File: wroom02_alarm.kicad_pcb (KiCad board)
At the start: 2 copper layers, 50 x 50 mm, 93 parts, among them J1 Serial, J10 pin, J11 pin, J12 pin, J13 pin, J14 pin, J15 pin, J2 pin, J3 microUSB, J4 pin, J5 pin, J6 pin, J7 pin, J8 pin, J9 pin, Q1 Q_NMOS_GDS, SW1 Write, SW2 RESET, U1 wroom02, U3 7803

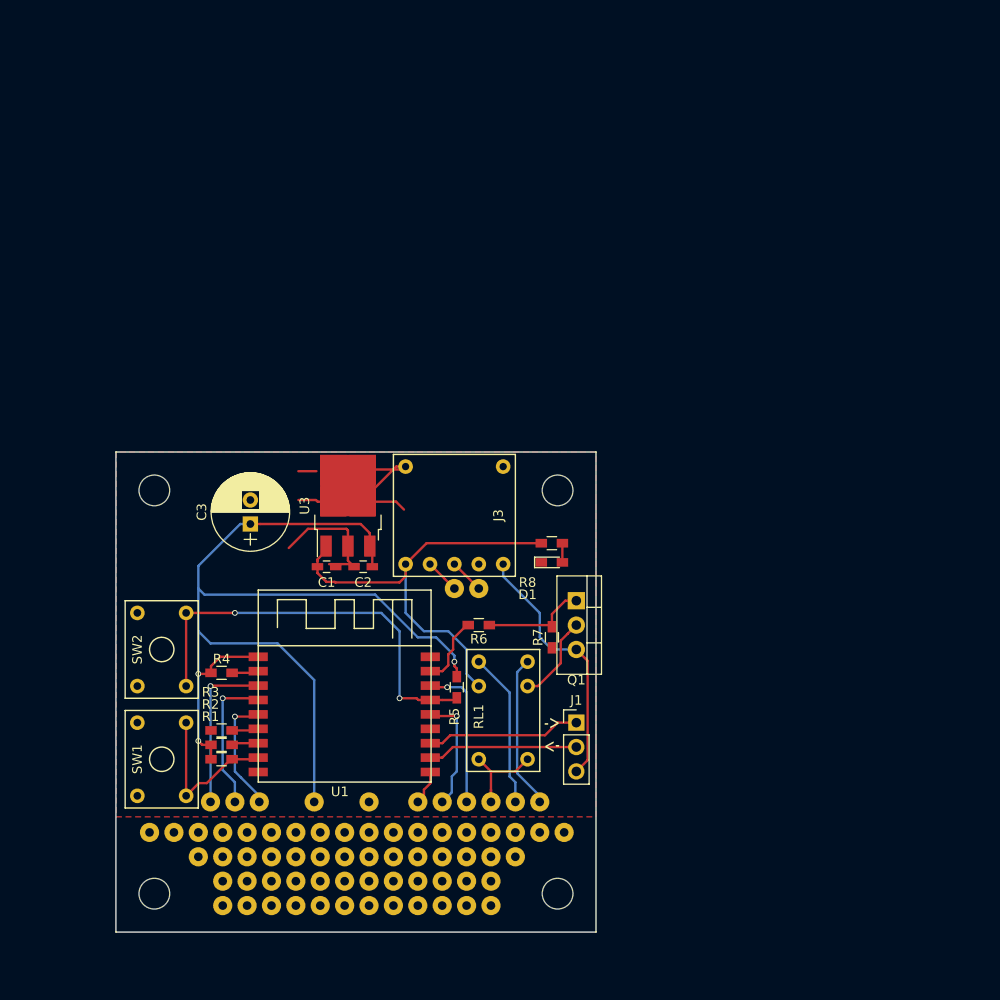
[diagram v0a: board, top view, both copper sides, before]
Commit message: 100x100に拡張
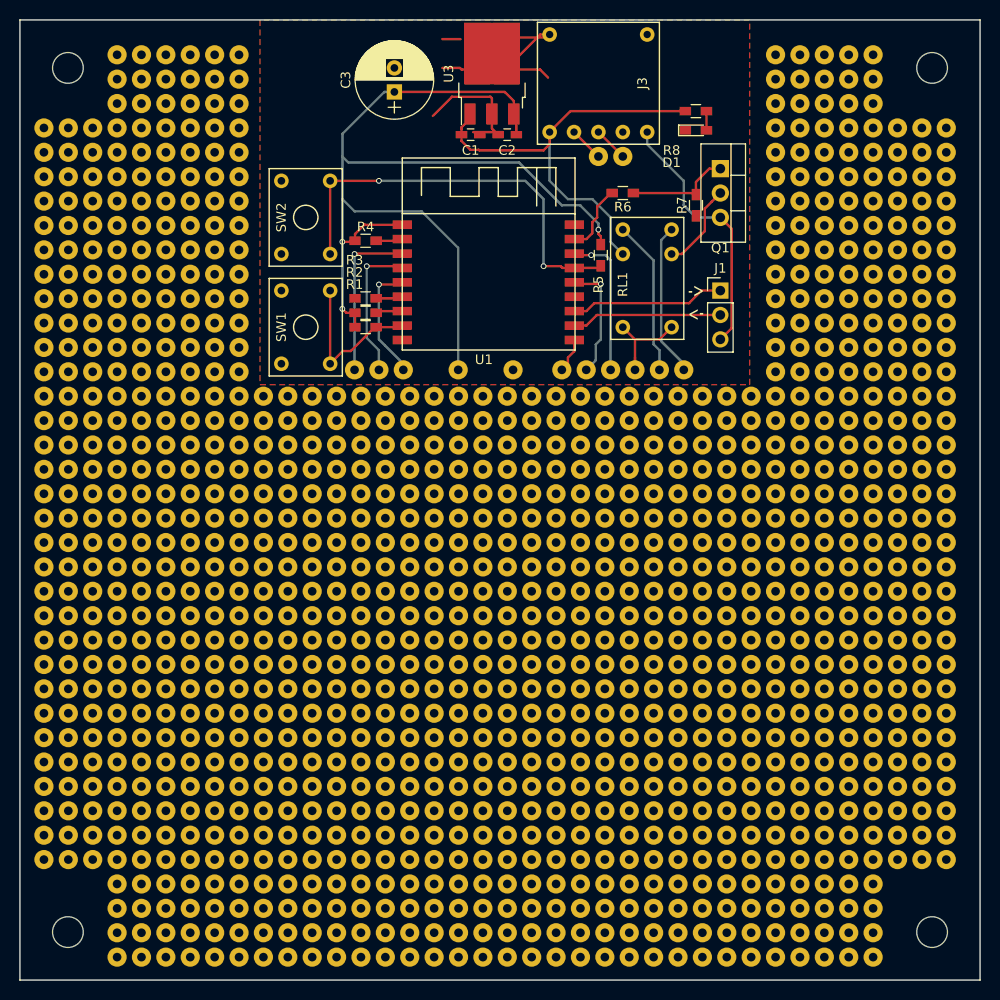
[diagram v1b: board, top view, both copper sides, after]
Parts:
- removed the REF** at (106.7, 134.6)
- removed the REF** at (101.6, 137.2)
- removed the REF** at (104.1, 134.6)
- removed the REF** at (101.6, 134.6)
- removed the REF** at (63.5, 134.6)
- removed the REF** at (66.0, 134.6)
- removed the REF** at (68.6, 137.2)
- removed the REF** at (68.6, 134.6)
- added REF**: , pad:universal, F.Cu at (72.8, 53.6)
- added REF**: , pad:universal, F.Cu at (67.7, 56.2)
- added REF**: , pad:universal, F.Cu at (57.6, 84.1)
- added REF**: , pad:universal, F.Cu at (128.7, 147.6)
- added REF**: , pad:universal, F.Cu at (126.2, 147.6)
- added REF**: , pad:universal, F.Cu at (126.2, 145.1)
- added REF**: , pad:universal, F.Cu at (131.2, 147.6)
- added REF**: , pad:universal, F.Cu at (128.7, 145.1)
- added REF**: , pad:universal, F.Cu at (133.8, 147.6)
- added REF**: , pad:universal, F.Cu at (133.8, 145.1)
- added REF**: , pad:universal, F.Cu at (133.8, 140.0)
- added REF**: , pad:universal, F.Cu at (133.8, 142.5)
- added REF**: , pad:universal, F.Cu at (121.1, 147.6)
- added REF**: , pad:universal, F.Cu at (57.6, 81.6)
- added REF**: , pad:universal, F.Cu at (123.6, 147.6)
- added REF**: , pad:universal, F.Cu at (123.6, 142.5)
- added REF**: , pad:universal, F.Cu at (123.6, 145.1)
- added REF**: , pad:universal, F.Cu at (105.8, 140.0)
- added REF**: , pad:universal, F.Cu at (108.4, 140.0)
- added REF**: , pad:universal, F.Cu at (108.4, 147.6)
- added REF**: , pad:universal, F.Cu at (105.8, 147.6)
- added REF**: , pad:universal, F.Cu at (105.8, 142.5)
- added REF**: , pad:universal, F.Cu at (108.4, 145.1)
- added REF**: , pad:universal, F.Cu at (105.8, 145.1)
- added REF**: , pad:universal, F.Cu at (60.1, 84.1)
- added REF**: , pad:universal, F.Cu at (108.4, 142.5)
- added REF**: , pad:universal, F.Cu at (110.9, 145.1)
- added REF**: , pad:universal, F.Cu at (113.5, 145.1)
- added REF**: , pad:universal, F.Cu at (116.0, 145.1)
- added REF**: , pad:universal, F.Cu at (116.0, 147.6)
- added REF**: , pad:universal, F.Cu at (113.5, 147.6)
- added REF**: , pad:universal, F.Cu at (110.9, 147.6)
- added REF**: , pad:universal, F.Cu at (118.5, 140.0)
- added REF**: , pad:universal, F.Cu at (118.5, 147.6)
- added REF**: , pad:universal, F.Cu at (118.5, 142.5)
- added REF**: , pad:universal, F.Cu at (60.1, 81.6)
- added REF**: , pad:universal, F.Cu at (118.5, 145.1)
- added REF**: , pad:universal, F.Cu at (110.9, 140.0)
- added REF**: , pad:universal, F.Cu at (116.0, 142.5)
- added REF**: , pad:universal, F.Cu at (116.0, 140.0)
- added REF**: , pad:universal, F.Cu at (113.5, 140.0)
- added REF**: , pad:universal, F.Cu at (113.5, 142.5)
- added REF**: , pad:universal, F.Cu at (110.9, 142.5)
- added REF**: , pad:universal, F.Cu at (90.6, 145.1)
- added REF**: , pad:universal, F.Cu at (90.6, 147.6)
- added REF**: , pad:universal, F.Cu at (90.6, 142.5)
- added REF**: , pad:universal, F.Cu at (60.1, 86.7)
- added REF**: , pad:universal, F.Cu at (90.6, 140.0)
- added REF**: , pad:universal, F.Cu at (98.2, 145.1)
- added REF**: , pad:universal, F.Cu at (100.8, 145.1)
- added REF**: , pad:universal, F.Cu at (103.3, 147.6)
- added REF**: , pad:universal, F.Cu at (103.3, 145.1)
- added REF**: , pad:universal, F.Cu at (100.8, 147.6)
- added REF**: , pad:universal, F.Cu at (98.2, 147.6)
- added REF**: , pad:universal, F.Cu at (93.1, 140.0)
- added REF**: , pad:universal, F.Cu at (93.1, 145.1)
- added REF**: , pad:universal, F.Cu at (95.7, 145.1)
- added REF**: , pad:universal, F.Cu at (55.0, 81.6)
- added REF**: , pad:universal, F.Cu at (93.1, 147.6)
- added REF**: , pad:universal, F.Cu at (95.7, 147.6)
- added REF**: , pad:universal, F.Cu at (93.1, 142.5)
- added REF**: , pad:universal, F.Cu at (95.7, 140.0)
- added REF**: , pad:universal, F.Cu at (98.2, 140.0)
- added REF**: , pad:universal, F.Cu at (98.2, 142.5)
- added REF**: , pad:universal, F.Cu at (100.8, 140.0)
- added REF**: , pad:universal, F.Cu at (103.3, 142.5)
- added REF**: , pad:universal, F.Cu at (103.3, 140.0)
- added REF**: , pad:universal, F.Cu at (95.7, 142.5)
- added REF**: , pad:universal, F.Cu at (55.0, 84.1)
- added REF**: , pad:universal, F.Cu at (100.8, 142.5)
- added REF**: , pad:universal, F.Cu at (52.5, 81.6)
- added REF**: , pad:universal, F.Cu at (52.5, 86.7)
- added REF**: , pad:universal, F.Cu at (52.5, 84.1)
- added REF**: , pad:universal, F.Cu at (65.2, 53.6)
- added REF**: , pad:universal, F.Cu at (70.3, 81.6)
- added REF**: , pad:universal, F.Cu at (70.3, 86.7)
- added REF**: , pad:universal, F.Cu at (72.8, 81.6)
- added REF**: , pad:universal, F.Cu at (70.3, 84.1)
- added REF**: , pad:universal, F.Cu at (72.8, 86.7)
- added REF**: , pad:universal, F.Cu at (72.8, 84.1)
- added REF**: , pad:universal, F.Cu at (55.0, 86.7)
- added REF**: , pad:universal, F.Cu at (57.6, 86.7)
- added REF**: , pad:universal, F.Cu at (133.8, 53.6)
- added REF**: , pad:universal, F.Cu at (133.8, 56.2)
- added REF**: , pad:universal, F.Cu at (65.2, 58.7)
- added REF**: , pad:universal, F.Cu at (138.9, 53.6)
- added REF**: , pad:universal, F.Cu at (136.3, 53.6)
- added REF**: , pad:universal, F.Cu at (133.8, 58.7)
- added REF**: , pad:universal, F.Cu at (138.9, 58.7)
- added REF**: , pad:universal, F.Cu at (136.3, 58.7)
- added REF**: , pad:universal, F.Cu at (136.3, 56.2)
- added REF**: , pad:universal, F.Cu at (138.9, 56.2)
- added REF**: , pad:universal, F.Cu at (131.2, 53.6)
- added REF**: , pad:universal, F.Cu at (131.2, 56.2)
- added REF**: , pad:universal, F.Cu at (128.7, 53.6)
- added REF**: , pad:universal, F.Cu at (60.1, 53.6)
- added REF**: , pad:universal, F.Cu at (131.2, 58.7)
- added REF**: , pad:universal, F.Cu at (128.7, 56.2)
- added REF**: , pad:universal, F.Cu at (128.7, 58.7)
- added REF**: , pad:universal, F.Cu at (143.9, 61.2)
- added REF**: , pad:universal, F.Cu at (141.4, 61.2)
- added REF**: , pad:universal, F.Cu at (146.5, 61.2)
- added REF**: , pad:universal, F.Cu at (136.3, 61.2)
- added REF**: , pad:universal, F.Cu at (138.9, 61.2)
- added REF**: , pad:universal, F.Cu at (128.7, 61.2)
- added REF**: , pad:universal, F.Cu at (133.8, 61.2)
- added REF**: , pad:universal, F.Cu at (62.7, 56.2)
- added REF**: , pad:universal, F.Cu at (131.2, 61.2)
- added REF**: , pad:universal, F.Cu at (133.8, 71.4)
- added REF**: , pad:universal, F.Cu at (131.2, 71.4)
- added REF**: , pad:universal, F.Cu at (128.7, 71.4)
- added REF**: , pad:universal, F.Cu at (131.2, 68.9)
- added REF**: , pad:universal, F.Cu at (128.7, 68.9)
- added REF**: , pad:universal, F.Cu at (133.8, 68.9)
- added REF**: , pad:universal, F.Cu at (143.9, 71.4)
- added REF**: , pad:universal, F.Cu at (146.5, 71.4)
- added REF**: , pad:universal, F.Cu at (141.4, 71.4)
- added REF**: , pad:universal, F.Cu at (60.1, 56.2)
- added REF**: , pad:universal, F.Cu at (146.5, 68.9)
- added REF**: , pad:universal, F.Cu at (141.4, 68.9)
- added REF**: , pad:universal, F.Cu at (141.4, 63.8)
- added REF**: , pad:universal, F.Cu at (143.9, 63.8)
- added REF**: , pad:universal, F.Cu at (143.9, 68.9)
- added REF**: , pad:universal, F.Cu at (141.4, 66.3)
- added REF**: , pad:universal, F.Cu at (143.9, 66.3)
- added REF**: , pad:universal, F.Cu at (128.7, 66.3)
- added REF**: , pad:universal, F.Cu at (128.7, 63.8)
- added REF**: , pad:universal, F.Cu at (131.2, 63.8)
- added REF**: , pad:universal, F.Cu at (62.7, 53.6)
- added REF**: , pad:universal, F.Cu at (131.2, 66.3)
- added REF**: , pad:universal, F.Cu at (133.8, 63.8)
- added REF**: , pad:universal, F.Cu at (133.8, 66.3)
- added REF**: , pad:universal, F.Cu at (138.9, 71.4)
- added REF**: , pad:universal, F.Cu at (138.9, 66.3)
- added REF**: , pad:universal, F.Cu at (136.3, 71.4)
- added REF**: , pad:universal, F.Cu at (138.9, 68.9)
- added REF**: , pad:universal, F.Cu at (136.3, 66.3)
- added REF**: , pad:universal, F.Cu at (136.3, 68.9)
- added REF**: , pad:universal, F.Cu at (138.9, 63.8)
- added REF**: , pad:universal, F.Cu at (62.7, 58.7)
- added REF**: , pad:universal, F.Cu at (146.5, 63.8)
- added REF**: , pad:universal, F.Cu at (136.3, 63.8)
- added REF**: , pad:universal, F.Cu at (146.5, 66.3)
- added REF**: , pad:universal, F.Cu at (136.3, 79.0)
- added REF**: , pad:universal, F.Cu at (133.8, 79.0)
- added REF**: , pad:universal, F.Cu at (133.8, 76.5)
- added REF**: , pad:universal, F.Cu at (133.8, 74.0)
- added REF**: , pad:universal, F.Cu at (136.3, 76.5)
- added REF**: , pad:universal, F.Cu at (131.2, 74.0)
- added REF**: , pad:universal, F.Cu at (128.7, 74.0)
- added REF**: , pad:universal, F.Cu at (60.1, 58.7)
- added REF**: , pad:universal, F.Cu at (131.2, 76.5)
- added REF**: , pad:universal, F.Cu at (146.5, 79.0)
- added REF**: , pad:universal, F.Cu at (146.5, 74.0)
- added REF**: , pad:universal, F.Cu at (146.5, 76.5)
- added REF**: , pad:universal, F.Cu at (143.9, 76.5)
- added REF**: , pad:universal, F.Cu at (141.4, 76.5)
- added REF**: , pad:universal, F.Cu at (143.9, 79.0)
- added REF**: , pad:universal, F.Cu at (141.4, 79.0)
- added REF**: , pad:universal, F.Cu at (143.9, 74.0)
- added REF**: , pad:universal, F.Cu at (141.4, 74.0)
- added REF**: , pad:universal, F.Cu at (72.8, 61.2)
- added REF**: , pad:universal, F.Cu at (138.9, 74.0)
- added REF**: , pad:universal, F.Cu at (136.3, 74.0)
- added REF**: , pad:universal, F.Cu at (138.9, 76.5)
- added REF**: , pad:universal, F.Cu at (138.9, 79.0)
- added REF**: , pad:universal, F.Cu at (128.7, 76.5)
- added REF**: , pad:universal, F.Cu at (128.7, 79.0)
- added REF**: , pad:universal, F.Cu at (131.2, 79.0)
- added REF**: , pad:universal, F.Cu at (131.2, 86.7)
- added REF**: , pad:universal, F.Cu at (133.8, 86.7)
- added REF**: , pad:universal, F.Cu at (128.7, 81.6)
- added REF**: , pad:universal, F.Cu at (70.3, 56.2)
- added REF**: , pad:universal, F.Cu at (70.3, 61.2)
- added REF**: , pad:universal, F.Cu at (131.2, 84.1)
- added REF**: , pad:universal, F.Cu at (133.8, 84.1)
- added REF**: , pad:universal, F.Cu at (131.2, 81.6)
- added REF**: , pad:universal, F.Cu at (133.8, 81.6)
- added REF**: , pad:universal, F.Cu at (128.7, 84.1)
- added REF**: , pad:universal, F.Cu at (128.7, 86.7)
- added REF**: , pad:universal, F.Cu at (141.4, 81.6)
- added REF**: , pad:universal, F.Cu at (146.5, 81.6)
- added REF**: , pad:universal, F.Cu at (143.9, 81.6)
- added REF**: , pad:universal, F.Cu at (146.5, 84.1)
- added REF**: , pad:universal, F.Cu at (67.7, 61.2)
- added REF**: , pad:universal, F.Cu at (143.9, 84.1)
- added REF**: , pad:universal, F.Cu at (143.9, 86.7)
- added REF**: , pad:universal, F.Cu at (141.4, 86.7)
- added REF**: , pad:universal, F.Cu at (141.4, 84.1)
- added REF**: , pad:universal, F.Cu at (146.5, 86.7)
- added REF**: , pad:universal, F.Cu at (136.3, 81.6)
- added REF**: , pad:universal, F.Cu at (138.9, 86.7)
- added REF**: , pad:universal, F.Cu at (136.3, 84.1)
- added REF**: , pad:universal, F.Cu at (136.3, 86.7)
- added REF**: , pad:universal, F.Cu at (138.9, 84.1)
- added REF**: , pad:universal, F.Cu at (52.5, 61.2)
- added REF**: , pad:universal, F.Cu at (138.9, 81.6)
- added REF**: , pad:universal, F.Cu at (136.3, 94.3)
- added REF**: , pad:universal, F.Cu at (136.3, 96.8)
- added REF**: , pad:universal, F.Cu at (146.5, 94.3)
- added REF**: , pad:universal, F.Cu at (143.9, 89.2)
- added REF**: , pad:universal, F.Cu at (146.5, 91.7)
- added REF**: , pad:universal, F.Cu at (146.5, 89.2)
- added REF**: , pad:universal, F.Cu at (143.9, 91.7)
- added REF**: , pad:universal, F.Cu at (138.9, 89.2)
- added REF**: , pad:universal, F.Cu at (136.3, 89.2)
- added REF**: , pad:universal, F.Cu at (57.6, 61.2)
- added REF**: , pad:universal, F.Cu at (141.4, 91.7)
- added REF**: , pad:universal, F.Cu at (141.4, 89.2)
- added REF**: , pad:universal, F.Cu at (136.3, 91.7)
- added REF**: , pad:universal, F.Cu at (138.9, 91.7)
- added REF**: , pad:universal, F.Cu at (138.9, 96.8)
- added REF**: , pad:universal, F.Cu at (143.9, 94.3)
- added REF**: , pad:universal, F.Cu at (141.4, 96.8)
- added REF**: , pad:universal, F.Cu at (141.4, 94.3)
- added REF**: , pad:universal, F.Cu at (138.9, 94.3)
- added REF**: , pad:universal, F.Cu at (146.5, 96.8)
- added REF**: , pad:universal, F.Cu at (55.0, 61.2)
- added REF**: , pad:universal, F.Cu at (143.9, 96.8)
- added REF**: , pad:universal, F.Cu at (133.8, 91.7)
- added REF**: , pad:universal, F.Cu at (131.2, 89.2)
- added REF**: , pad:universal, F.Cu at (131.2, 91.7)
- added REF**: , pad:universal, F.Cu at (133.8, 89.2)
- added REF**: , pad:universal, F.Cu at (121.1, 94.3)
- added REF**: , pad:universal, F.Cu at (121.1, 96.8)
- added REF**: , pad:universal, F.Cu at (123.6, 94.3)
- added REF**: , pad:universal, F.Cu at (123.6, 96.8)
- added REF**: , pad:universal, F.Cu at (126.2, 94.3)
- added REF**: , pad:universal, F.Cu at (60.1, 61.2)
- added REF**: , pad:universal, F.Cu at (128.7, 96.8)
- added REF**: , pad:universal, F.Cu at (126.2, 96.8)
- added REF**: , pad:universal, F.Cu at (128.7, 94.3)
- added REF**: , pad:universal, F.Cu at (121.1, 91.7)
- added REF**: , pad:universal, F.Cu at (121.1, 89.2)
- added REF**: , pad:universal, F.Cu at (128.7, 89.2)
- added REF**: , pad:universal, F.Cu at (126.2, 91.7)
- added REF**: , pad:universal, F.Cu at (128.7, 91.7)
- added REF**: , pad:universal, F.Cu at (123.6, 91.7)
- added REF**: , pad:universal, F.Cu at (123.6, 89.2)
- added REF**: , pad:universal, F.Cu at (62.7, 61.2)
- added REF**: , pad:universal, F.Cu at (126.2, 89.2)
- added REF**: , pad:universal, F.Cu at (133.8, 94.3)
- added REF**: , pad:universal, F.Cu at (133.8, 96.8)
- added REF**: , pad:universal, F.Cu at (131.2, 96.8)
- added REF**: , pad:universal, F.Cu at (131.2, 94.3)
- added REF**: , pad:universal, F.Cu at (88.1, 89.2)
- added REF**: , pad:universal, F.Cu at (88.1, 91.7)
- added REF**: , pad:universal, F.Cu at (85.5, 89.2)
- added REF**: , pad:universal, F.Cu at (85.5, 91.7)
- added REF**: , pad:universal, F.Cu at (67.7, 89.2)
- added REF**: , pad:universal, F.Cu at (65.2, 61.2)
- added REF**: , pad:universal, F.Cu at (67.7, 91.7)
- added REF**: , pad:universal, F.Cu at (70.3, 91.7)
- added REF**: , pad:universal, F.Cu at (70.3, 89.2)
- added REF**: , pad:universal, F.Cu at (83.0, 91.7)
- added REF**: , pad:universal, F.Cu at (83.0, 89.2)
- added REF**: , pad:universal, F.Cu at (77.9, 91.7)
- added REF**: , pad:universal, F.Cu at (77.9, 94.3)
- added REF**: , pad:universal, F.Cu at (80.4, 91.7)
- added REF**: , pad:universal, F.Cu at (80.4, 89.2)
- added REF**: , pad:universal, F.Cu at (77.9, 89.2)
- added REF**: , pad:universal, F.Cu at (67.7, 63.8)
- added REF**: , pad:universal, F.Cu at (70.3, 94.3)
- added REF**: , pad:universal, F.Cu at (72.8, 89.2)
- added REF**: , pad:universal, F.Cu at (75.4, 91.7)
- added REF**: , pad:universal, F.Cu at (75.4, 94.3)
- added REF**: , pad:universal, F.Cu at (75.4, 89.2)
- added REF**: , pad:universal, F.Cu at (72.8, 94.3)
- added REF**: , pad:universal, F.Cu at (72.8, 91.7)
- added REF**: , pad:universal, F.Cu at (75.4, 96.8)
- added REF**: , pad:universal, F.Cu at (77.9, 96.8)
- added REF**: , pad:universal, F.Cu at (65.2, 96.8)
- added REF**: , pad:universal, F.Cu at (70.3, 66.3)
- added REF**: , pad:universal, F.Cu at (67.7, 96.8)
- added REF**: , pad:universal, F.Cu at (72.8, 96.8)
- added REF**: , pad:universal, F.Cu at (70.3, 96.8)
- added REF**: , pad:universal, F.Cu at (67.7, 94.3)
- added REF**: , pad:universal, F.Cu at (65.2, 89.2)
- added REF**: , pad:universal, F.Cu at (65.2, 91.7)
- added REF**: , pad:universal, F.Cu at (65.2, 94.3)
- added REF**: , pad:universal, F.Cu at (57.6, 96.8)
- added REF**: , pad:universal, F.Cu at (60.1, 94.3)
- added REF**: , pad:universal, F.Cu at (57.6, 94.3)
- added REF**: , pad:universal, F.Cu at (72.8, 56.2)
- added REF**: , pad:universal, F.Cu at (72.8, 66.3)
- added REF**: , pad:universal, F.Cu at (62.7, 89.2)
- added REF**: , pad:universal, F.Cu at (60.1, 89.2)
- added REF**: , pad:universal, F.Cu at (60.1, 91.7)
- added REF**: , pad:universal, F.Cu at (62.7, 91.7)
- added REF**: , pad:universal, F.Cu at (62.7, 94.3)
- added REF**: , pad:universal, F.Cu at (62.7, 96.8)
- added REF**: , pad:universal, F.Cu at (60.1, 96.8)
- added REF**: , pad:universal, F.Cu at (52.5, 91.7)
- added REF**: , pad:universal, F.Cu at (55.0, 94.3)
- added REF**: , pad:universal, F.Cu at (52.5, 94.3)
- added REF**: , pad:universal, F.Cu at (67.7, 66.3)
- added REF**: , pad:universal, F.Cu at (52.5, 89.2)
- added REF**: , pad:universal, F.Cu at (55.0, 96.8)
- added REF**: , pad:universal, F.Cu at (52.5, 96.8)
- added REF**: , pad:universal, F.Cu at (57.6, 89.2)
- added REF**: , pad:universal, F.Cu at (55.0, 89.2)
- added REF**: , pad:universal, F.Cu at (57.6, 91.7)
- added REF**: , pad:universal, F.Cu at (55.0, 91.7)
- added REF**: , pad:universal, F.Cu at (80.4, 94.3)
- added REF**: , pad:universal, F.Cu at (83.0, 94.3)
- added REF**: , pad:universal, F.Cu at (83.0, 96.8)
- added REF**: , pad:universal, F.Cu at (70.3, 63.8)
- added REF**: , pad:universal, F.Cu at (80.4, 96.8)
- added REF**: , pad:universal, F.Cu at (85.5, 94.3)
- added REF**: , pad:universal, F.Cu at (88.1, 94.3)
- added REF**: , pad:universal, F.Cu at (88.1, 96.8)
- added REF**: , pad:universal, F.Cu at (85.5, 96.8)
- added REF**: , pad:universal, F.Cu at (90.6, 96.8)
- added REF**: , pad:universal, F.Cu at (93.1, 94.3)
- added REF**: , pad:universal, F.Cu at (93.1, 96.8)
- added REF**: , pad:universal, F.Cu at (90.6, 94.3)
- added REF**: , pad:universal, F.Cu at (90.6, 91.7)
- added REF**: , pad:universal, F.Cu at (72.8, 63.8)
- added REF**: , pad:universal, F.Cu at (93.1, 91.7)
- added REF**: , pad:universal, F.Cu at (93.1, 89.2)
- added REF**: , pad:universal, F.Cu at (90.6, 89.2)
- added REF**: , pad:universal, F.Cu at (95.7, 91.7)
- added REF**: , pad:universal, F.Cu at (100.8, 89.2)
- added REF**: , pad:universal, F.Cu at (100.8, 91.7)
- added REF**: , pad:universal, F.Cu at (98.2, 91.7)
- added REF**: , pad:universal, F.Cu at (95.7, 89.2)
- added REF**: , pad:universal, F.Cu at (98.2, 89.2)
- added REF**: , pad:universal, F.Cu at (103.3, 96.8)
- added REF**: , pad:universal, F.Cu at (62.7, 66.3)
- added REF**: , pad:universal, F.Cu at (105.8, 96.8)
- added REF**: , pad:universal, F.Cu at (105.8, 94.3)
- added REF**: , pad:universal, F.Cu at (103.3, 94.3)
- added REF**: , pad:universal, F.Cu at (103.3, 89.2)
- added REF**: , pad:universal, F.Cu at (105.8, 89.2)
- added REF**: , pad:universal, F.Cu at (103.3, 91.7)
- added REF**: , pad:universal, F.Cu at (105.8, 91.7)
- added REF**: , pad:universal, F.Cu at (95.7, 94.3)
- added REF**: , pad:universal, F.Cu at (98.2, 96.8)
- added REF**: , pad:universal, F.Cu at (95.7, 96.8)
- added REF**: , pad:universal, F.Cu at (65.2, 63.8)
- added REF**: , pad:universal, F.Cu at (100.8, 94.3)
- added REF**: , pad:universal, F.Cu at (100.8, 96.8)
- added REF**: , pad:universal, F.Cu at (98.2, 94.3)
- added REF**: , pad:universal, F.Cu at (118.5, 94.3)
- added REF**: , pad:universal, F.Cu at (116.0, 96.8)
- added REF**: , pad:universal, F.Cu at (116.0, 94.3)
- added REF**: , pad:universal, F.Cu at (118.5, 96.8)
- added REF**: , pad:universal, F.Cu at (118.5, 91.7)
- added REF**: , pad:universal, F.Cu at (116.0, 89.2)
- added REF**: , pad:universal, F.Cu at (116.0, 91.7)
- added REF**: , pad:universal, F.Cu at (65.2, 66.3)
- added REF**: , pad:universal, F.Cu at (118.5, 89.2)
- added REF**: , pad:universal, F.Cu at (113.5, 96.8)
- added REF**: , pad:universal, F.Cu at (108.4, 94.3)
- added REF**: , pad:universal, F.Cu at (110.9, 96.8)
- added REF**: , pad:universal, F.Cu at (113.5, 94.3)
- added REF**: , pad:universal, F.Cu at (110.9, 94.3)
- added REF**: , pad:universal, F.Cu at (108.4, 96.8)
- added REF**: , pad:universal, F.Cu at (108.4, 91.7)
- added REF**: , pad:universal, F.Cu at (113.5, 91.7)
- added REF**: , pad:universal, F.Cu at (113.5, 89.2)
- added REF**: , pad:universal, F.Cu at (62.7, 63.8)
- added REF**: , pad:universal, F.Cu at (110.9, 89.2)
- added REF**: , pad:universal, F.Cu at (110.9, 91.7)
- added REF**: , pad:universal, F.Cu at (108.4, 89.2)
- added REF**: , pad:universal, F.Cu at (60.1, 104.4)
- added REF**: , pad:universal, F.Cu at (62.7, 104.4)
- added REF**: , pad:universal, F.Cu at (60.1, 101.9)
- added REF**: , pad:universal, F.Cu at (60.1, 99.3)
- added REF**: , pad:universal, F.Cu at (62.7, 101.9)
- added REF**: , pad:universal, F.Cu at (62.7, 99.3)
- added REF**: , pad:universal, F.Cu at (52.5, 114.6)
- added REF**: , pad:universal, F.Cu at (60.1, 63.8)
- added REF**: , pad:universal, F.Cu at (52.5, 117.1)
- added REF**: , pad:universal, F.Cu at (55.0, 117.1)
- added REF**: , pad:universal, F.Cu at (55.0, 114.6)
- added REF**: , pad:universal, F.Cu at (60.1, 117.1)
- added REF**: , pad:universal, F.Cu at (62.7, 114.6)
- added REF**: , pad:universal, F.Cu at (62.7, 117.1)
- added REF**: , pad:universal, F.Cu at (60.1, 114.6)
- added REF**: , pad:universal, F.Cu at (55.0, 101.9)
- added REF**: , pad:universal, F.Cu at (57.6, 101.9)
- added REF**: , pad:universal, F.Cu at (52.5, 99.3)
- added REF**: , pad:universal, F.Cu at (60.1, 66.3)
- added REF**: , pad:universal, F.Cu at (57.6, 99.3)
- added REF**: , pad:universal, F.Cu at (52.5, 101.9)
- added REF**: , pad:universal, F.Cu at (55.0, 99.3)
- added REF**: , pad:universal, F.Cu at (57.6, 114.6)
- added REF**: , pad:universal, F.Cu at (57.6, 117.1)
- added REF**: , pad:universal, F.Cu at (55.0, 112.0)
- added REF**: , pad:universal, F.Cu at (52.5, 112.0)
- added REF**: , pad:universal, F.Cu at (55.0, 104.4)
- added REF**: , pad:universal, F.Cu at (52.5, 104.4)
- added REF**: , pad:universal, F.Cu at (57.6, 104.4)
- added REF**: , pad:universal, F.Cu at (72.8, 58.7)
- added REF**: , pad:universal, F.Cu at (52.5, 66.3)
- added REF**: , pad:universal, F.Cu at (52.5, 107.0)
- added REF**: , pad:universal, F.Cu at (52.5, 109.5)
- added REF**: , pad:universal, F.Cu at (55.0, 107.0)
- added REF**: , pad:universal, F.Cu at (55.0, 109.5)
- added REF**: , pad:universal, F.Cu at (57.6, 109.5)
- added REF**: , pad:universal, F.Cu at (57.6, 107.0)
- added REF**: , pad:universal, F.Cu at (60.1, 107.0)
- added REF**: , pad:universal, F.Cu at (62.7, 107.0)
- added REF**: , pad:universal, F.Cu at (62.7, 112.0)
- added REF**: , pad:universal, F.Cu at (62.7, 109.5)
- added REF**: , pad:universal, F.Cu at (55.0, 63.8)
- added REF**: , pad:universal, F.Cu at (60.1, 109.5)
- added REF**: , pad:universal, F.Cu at (57.6, 112.0)
- added REF**: , pad:universal, F.Cu at (60.1, 112.0)
- added REF**: , pad:universal, F.Cu at (77.9, 117.1)
- added REF**: , pad:universal, F.Cu at (77.9, 114.6)
- added REF**: , pad:universal, F.Cu at (70.3, 117.1)
- added REF**: , pad:universal, F.Cu at (65.2, 117.1)
- added REF**: , pad:universal, F.Cu at (67.7, 117.1)
- added REF**: , pad:universal, F.Cu at (70.3, 109.5)
- added REF**: , pad:universal, F.Cu at (65.2, 114.6)
- added REF**: , pad:universal, F.Cu at (57.6, 63.8)
- added REF**: , pad:universal, F.Cu at (70.3, 114.6)
- added REF**: , pad:universal, F.Cu at (67.7, 114.6)
- added REF**: , pad:universal, F.Cu at (70.3, 112.0)
- added REF**: , pad:universal, F.Cu at (67.7, 112.0)
- added REF**: , pad:universal, F.Cu at (65.2, 109.5)
- added REF**: , pad:universal, F.Cu at (67.7, 109.5)
- added REF**: , pad:universal, F.Cu at (65.2, 112.0)
- added REF**: , pad:universal, F.Cu at (75.4, 114.6)
- added REF**: , pad:universal, F.Cu at (72.8, 117.1)
- added REF**: , pad:universal, F.Cu at (75.4, 117.1)
- added REF**: , pad:universal, F.Cu at (55.0, 66.3)
- added REF**: , pad:universal, F.Cu at (72.8, 114.6)
- added REF**: , pad:universal, F.Cu at (77.9, 109.5)
- added REF**: , pad:universal, F.Cu at (72.8, 109.5)
- added REF**: , pad:universal, F.Cu at (75.4, 109.5)
- added REF**: , pad:universal, F.Cu at (75.4, 112.0)
- added REF**: , pad:universal, F.Cu at (77.9, 112.0)
- added REF**: , pad:universal, F.Cu at (72.8, 112.0)
- added REF**: , pad:universal, F.Cu at (85.5, 104.4)
- added REF**: , pad:universal, F.Cu at (85.5, 107.0)
- added REF**: , pad:universal, F.Cu at (88.1, 107.0)
- added REF**: , pad:universal, F.Cu at (52.5, 63.8)
- added REF**: , pad:universal, F.Cu at (88.1, 104.4)
- added REF**: , pad:universal, F.Cu at (88.1, 101.9)
- added REF**: , pad:universal, F.Cu at (70.3, 101.9)
- added REF**: , pad:universal, F.Cu at (67.7, 99.3)
- added REF**: , pad:universal, F.Cu at (67.7, 101.9)
- added REF**: , pad:universal, F.Cu at (72.8, 101.9)
- added REF**: , pad:universal, F.Cu at (72.8, 99.3)
- added REF**: , pad:universal, F.Cu at (70.3, 99.3)
- added REF**: , pad:universal, F.Cu at (75.4, 99.3)
- added REF**: , pad:universal, F.Cu at (77.9, 99.3)
- added REF**: , pad:universal, F.Cu at (57.6, 66.3)
- added REF**: , pad:universal, F.Cu at (75.4, 101.9)
- added REF**: , pad:universal, F.Cu at (77.9, 101.9)
- added REF**: , pad:universal, F.Cu at (80.4, 99.3)
- added REF**: , pad:universal, F.Cu at (70.3, 107.0)
- added REF**: , pad:universal, F.Cu at (72.8, 104.4)
- added REF**: , pad:universal, F.Cu at (72.8, 107.0)
- added REF**: , pad:universal, F.Cu at (75.4, 107.0)
- added REF**: , pad:universal, F.Cu at (75.4, 104.4)
- added REF**: , pad:universal, F.Cu at (70.3, 104.4)
- added REF**: , pad:universal, F.Cu at (67.7, 107.0)
- added REF**: , pad:universal, F.Cu at (67.7, 71.4)
- added REF**: , pad:universal, F.Cu at (65.2, 101.9)
- added REF**: , pad:universal, F.Cu at (65.2, 99.3)
- added REF**: , pad:universal, F.Cu at (67.7, 104.4)
- added REF**: , pad:universal, F.Cu at (65.2, 104.4)
- added REF**: , pad:universal, F.Cu at (65.2, 107.0)
- added REF**: , pad:universal, F.Cu at (77.9, 104.4)
- added REF**: , pad:universal, F.Cu at (77.9, 107.0)
- added REF**: , pad:universal, F.Cu at (83.0, 107.0)
- added REF**: , pad:universal, F.Cu at (80.4, 101.9)
- added REF**: , pad:universal, F.Cu at (80.4, 104.4)
- added REF**: , pad:universal, F.Cu at (65.2, 74.0)
- added REF**: , pad:universal, F.Cu at (80.4, 107.0)
- added REF**: , pad:universal, F.Cu at (83.0, 104.4)
- added REF**: , pad:universal, F.Cu at (85.5, 99.3)
- added REF**: , pad:universal, F.Cu at (88.1, 99.3)
- added REF**: , pad:universal, F.Cu at (83.0, 99.3)
- added REF**: , pad:universal, F.Cu at (85.5, 101.9)
- added REF**: , pad:universal, F.Cu at (83.0, 101.9)
- added REF**: , pad:universal, F.Cu at (116.0, 117.1)
- added REF**: , pad:universal, F.Cu at (116.0, 114.6)
- added REF**: , pad:universal, F.Cu at (118.5, 117.1)
- added REF**: , pad:universal, F.Cu at (67.7, 74.0)
- added REF**: , pad:universal, F.Cu at (118.5, 114.6)
- added REF**: , pad:universal, F.Cu at (113.5, 117.1)
- added REF**: , pad:universal, F.Cu at (110.9, 114.6)
- added REF**: , pad:universal, F.Cu at (113.5, 114.6)
- added REF**: , pad:universal, F.Cu at (110.9, 117.1)
- added REF**: , pad:universal, F.Cu at (110.9, 109.5)
- added REF**: , pad:universal, F.Cu at (110.9, 112.0)
- added REF**: , pad:universal, F.Cu at (113.5, 112.0)
- added REF**: , pad:universal, F.Cu at (113.5, 109.5)
- added REF**: , pad:universal, F.Cu at (116.0, 112.0)
- added REF**: , pad:universal, F.Cu at (67.7, 68.9)
- added REF**: , pad:universal, F.Cu at (116.0, 109.5)
- added REF**: , pad:universal, F.Cu at (118.5, 109.5)
- added REF**: , pad:universal, F.Cu at (118.5, 112.0)
- added REF**: , pad:universal, F.Cu at (123.6, 117.1)
- added REF**: , pad:universal, F.Cu at (121.1, 114.6)
- added REF**: , pad:universal, F.Cu at (121.1, 117.1)
- added REF**: , pad:universal, F.Cu at (123.6, 114.6)
- added REF**: , pad:universal, F.Cu at (136.3, 109.5)
- added REF**: , pad:universal, F.Cu at (131.2, 109.5)
- added REF**: , pad:universal, F.Cu at (133.8, 112.0)
- added REF**: , pad:universal, F.Cu at (70.3, 53.6)
- added REF**: , pad:universal, F.Cu at (65.2, 71.4)
- added REF**: , pad:universal, F.Cu at (131.2, 112.0)
- added REF**: , pad:universal, F.Cu at (133.8, 109.5)
- added REF**: , pad:universal, F.Cu at (133.8, 114.6)
- added REF**: , pad:universal, F.Cu at (136.3, 117.1)
- added REF**: , pad:universal, F.Cu at (133.8, 117.1)
- added REF**: , pad:universal, F.Cu at (136.3, 112.0)
- added REF**: , pad:universal, F.Cu at (136.3, 114.6)
- added REF**: , pad:universal, F.Cu at (123.6, 109.5)
- added REF**: , pad:universal, F.Cu at (123.6, 112.0)
- added REF**: , pad:universal, F.Cu at (121.1, 109.5)
- added REF**: , pad:universal, F.Cu at (62.7, 68.9)
- added REF**: , pad:universal, F.Cu at (121.1, 112.0)
- added REF**: , pad:universal, F.Cu at (126.2, 109.5)
- added REF**: , pad:universal, F.Cu at (128.7, 112.0)
- added REF**: , pad:universal, F.Cu at (128.7, 109.5)
- added REF**: , pad:universal, F.Cu at (126.2, 112.0)
- added REF**: , pad:universal, F.Cu at (126.2, 114.6)
- added REF**: , pad:universal, F.Cu at (126.2, 117.1)
- added REF**: , pad:universal, F.Cu at (131.2, 114.6)
- added REF**: , pad:universal, F.Cu at (128.7, 114.6)
- added REF**: , pad:universal, F.Cu at (131.2, 117.1)
- added REF**: , pad:universal, F.Cu at (65.2, 68.9)
- added REF**: , pad:universal, F.Cu at (128.7, 117.1)
- added REF**: , pad:universal, F.Cu at (108.4, 101.9)
- added REF**: , pad:universal, F.Cu at (108.4, 99.3)
- added REF**: , pad:universal, F.Cu at (110.9, 99.3)
- added REF**: , pad:universal, F.Cu at (113.5, 99.3)
- added REF**: , pad:universal, F.Cu at (110.9, 101.9)
- added REF**: , pad:universal, F.Cu at (113.5, 101.9)
- added REF**: , pad:universal, F.Cu at (116.0, 107.0)
- added REF**: , pad:universal, F.Cu at (121.1, 104.4)
- added REF**: , pad:universal, F.Cu at (116.0, 104.4)
- added REF**: , pad:universal, F.Cu at (62.7, 71.4)
- added REF**: , pad:universal, F.Cu at (123.6, 104.4)
- added REF**: , pad:universal, F.Cu at (123.6, 107.0)
- added REF**: , pad:universal, F.Cu at (121.1, 107.0)
- added REF**: , pad:universal, F.Cu at (118.5, 107.0)
- added REF**: , pad:universal, F.Cu at (118.5, 104.4)
- added REF**: , pad:universal, F.Cu at (126.2, 101.9)
- added REF**: , pad:universal, F.Cu at (128.7, 107.0)
- added REF**: , pad:universal, F.Cu at (128.7, 104.4)
- added REF**: , pad:universal, F.Cu at (126.2, 104.4)
- added REF**: , pad:universal, F.Cu at (128.7, 101.9)
- added REF**: , pad:universal, F.Cu at (62.7, 74.0)
- added REF**: , pad:universal, F.Cu at (126.2, 99.3)
- added REF**: , pad:universal, F.Cu at (128.7, 99.3)
- added REF**: , pad:universal, F.Cu at (126.2, 107.0)
- added REF**: , pad:universal, F.Cu at (116.0, 99.3)
- added REF**: , pad:universal, F.Cu at (116.0, 101.9)
- added REF**: , pad:universal, F.Cu at (121.1, 101.9)
- added REF**: , pad:universal, F.Cu at (123.6, 101.9)
- added REF**: , pad:universal, F.Cu at (123.6, 99.3)
- added REF**: , pad:universal, F.Cu at (121.1, 99.3)
- added REF**: , pad:universal, F.Cu at (118.5, 99.3)
- added REF**: , pad:universal, F.Cu at (57.6, 71.4)
- added REF**: , pad:universal, F.Cu at (118.5, 101.9)
- added REF**: , pad:universal, F.Cu at (108.4, 107.0)
- added REF**: , pad:universal, F.Cu at (113.5, 107.0)
- added REF**: , pad:universal, F.Cu at (110.9, 107.0)
- added REF**: , pad:universal, F.Cu at (108.4, 104.4)
- added REF**: , pad:universal, F.Cu at (110.9, 104.4)
- added REF**: , pad:universal, F.Cu at (113.5, 104.4)
- added REF**: , pad:universal, F.Cu at (146.5, 101.9)
- added REF**: , pad:universal, F.Cu at (146.5, 107.0)
- added REF**: , pad:universal, F.Cu at (146.5, 104.4)
- added REF**: , pad:universal, F.Cu at (57.6, 68.9)
- added REF**: , pad:universal, F.Cu at (146.5, 99.3)
- added REF**: , pad:universal, F.Cu at (143.9, 99.3)
- added REF**: , pad:universal, F.Cu at (136.3, 99.3)
- added REF**: , pad:universal, F.Cu at (136.3, 101.9)
- added REF**: , pad:universal, F.Cu at (133.8, 99.3)
- added REF**: , pad:universal, F.Cu at (131.2, 99.3)
- added REF**: , pad:universal, F.Cu at (136.3, 107.0)
- added REF**: , pad:universal, F.Cu at (133.8, 107.0)
- added REF**: , pad:universal, F.Cu at (136.3, 104.4)
- added REF**: , pad:universal, F.Cu at (133.8, 104.4)
- added REF**: , pad:universal, F.Cu at (60.1, 71.4)
- added REF**: , pad:universal, F.Cu at (133.8, 101.9)
- added REF**: , pad:universal, F.Cu at (131.2, 104.4)
- added REF**: , pad:universal, F.Cu at (131.2, 101.9)
- added REF**: , pad:universal, F.Cu at (131.2, 107.0)
- added REF**: , pad:universal, F.Cu at (141.4, 101.9)
- added REF**: , pad:universal, F.Cu at (138.9, 101.9)
- added REF**: , pad:universal, F.Cu at (141.4, 99.3)
- added REF**: , pad:universal, F.Cu at (138.9, 99.3)
- added REF**: , pad:universal, F.Cu at (143.9, 104.4)
- added REF**: , pad:universal, F.Cu at (143.9, 101.9)
- added REF**: , pad:universal, F.Cu at (60.1, 68.9)
- added REF**: , pad:universal, F.Cu at (141.4, 104.4)
- added REF**: , pad:universal, F.Cu at (138.9, 104.4)
- added REF**: , pad:universal, F.Cu at (138.9, 109.5)
- added REF**: , pad:universal, F.Cu at (138.9, 112.0)
- added REF**: , pad:universal, F.Cu at (138.9, 107.0)
- added REF**: , pad:universal, F.Cu at (141.4, 109.5)
- added REF**: , pad:universal, F.Cu at (143.9, 107.0)
- added REF**: , pad:universal, F.Cu at (141.4, 107.0)
- added REF**: , pad:universal, F.Cu at (141.4, 112.0)
- added REF**: , pad:universal, F.Cu at (105.8, 107.0)
- added REF**: , pad:universal, F.Cu at (60.1, 74.0)
- added REF**: , pad:universal, F.Cu at (103.3, 107.0)
- added REF**: , pad:universal, F.Cu at (100.8, 107.0)
- added REF**: , pad:universal, F.Cu at (100.8, 104.4)
- added REF**: , pad:universal, F.Cu at (100.8, 101.9)
- added REF**: , pad:universal, F.Cu at (98.2, 99.3)
- added REF**: , pad:universal, F.Cu at (98.2, 101.9)
- added REF**: , pad:universal, F.Cu at (98.2, 104.4)
- added REF**: , pad:universal, F.Cu at (100.8, 99.3)
- added REF**: , pad:universal, F.Cu at (90.6, 99.3)
- added REF**: , pad:universal, F.Cu at (95.7, 99.3)
- added REF**: , pad:universal, F.Cu at (70.3, 58.7)
- added REF**: , pad:universal, F.Cu at (55.0, 68.9)
- added REF**: , pad:universal, F.Cu at (93.1, 101.9)
- added REF**: , pad:universal, F.Cu at (90.6, 101.9)
- added REF**: , pad:universal, F.Cu at (95.7, 101.9)
- added REF**: , pad:universal, F.Cu at (93.1, 99.3)
- added REF**: , pad:universal, F.Cu at (105.8, 101.9)
- added REF**: , pad:universal, F.Cu at (105.8, 104.4)
- added REF**: , pad:universal, F.Cu at (103.3, 99.3)
- added REF**: , pad:universal, F.Cu at (105.8, 99.3)
- added REF**: , pad:universal, F.Cu at (103.3, 101.9)
- added REF**: , pad:universal, F.Cu at (103.3, 104.4)
- added REF**: , pad:universal, F.Cu at (55.0, 71.4)
- added REF**: , pad:universal, F.Cu at (98.2, 107.0)
- added REF**: , pad:universal, F.Cu at (90.6, 104.4)
- added REF**: , pad:universal, F.Cu at (95.7, 107.0)
- added REF**: , pad:universal, F.Cu at (93.1, 107.0)
- added REF**: , pad:universal, F.Cu at (90.6, 107.0)
- added REF**: , pad:universal, F.Cu at (95.7, 104.4)
- added REF**: , pad:universal, F.Cu at (93.1, 104.4)
- added REF**: , pad:universal, F.Cu at (146.5, 109.5)
- added REF**: , pad:universal, F.Cu at (146.5, 114.6)
- added REF**: , pad:universal, F.Cu at (143.9, 109.5)
- added REF**: , pad:universal, F.Cu at (52.5, 68.9)
- added REF**: , pad:universal, F.Cu at (146.5, 112.0)
- added REF**: , pad:universal, F.Cu at (143.9, 112.0)
- added REF**: , pad:universal, F.Cu at (138.9, 114.6)
- added REF**: , pad:universal, F.Cu at (141.4, 114.6)
- added REF**: , pad:universal, F.Cu at (143.9, 114.6)
- added REF**: , pad:universal, F.Cu at (138.9, 117.1)
- added REF**: , pad:universal, F.Cu at (143.9, 117.1)
- added REF**: , pad:universal, F.Cu at (141.4, 117.1)
- added REF**: , pad:universal, F.Cu at (146.5, 117.1)
- added REF**: , pad:universal, F.Cu at (100.8, 117.1)
- added REF**: , pad:universal, F.Cu at (52.5, 74.0)
- added REF**: , pad:universal, F.Cu at (103.3, 117.1)
- added REF**: , pad:universal, F.Cu at (100.8, 114.6)
- added REF**: , pad:universal, F.Cu at (103.3, 114.6)
- added REF**: , pad:universal, F.Cu at (105.8, 109.5)
- added REF**: , pad:universal, F.Cu at (108.4, 112.0)
- added REF**: , pad:universal, F.Cu at (105.8, 112.0)
- added REF**: , pad:universal, F.Cu at (108.4, 109.5)
- added REF**: , pad:universal, F.Cu at (108.4, 114.6)
- added REF**: , pad:universal, F.Cu at (105.8, 117.1)
- added REF**: , pad:universal, F.Cu at (105.8, 114.6)
- added REF**: , pad:universal, F.Cu at (52.5, 71.4)
- added REF**: , pad:universal, F.Cu at (108.4, 117.1)
- added REF**: , pad:universal, F.Cu at (100.8, 109.5)
- added REF**: , pad:universal, F.Cu at (100.8, 112.0)
- added REF**: , pad:universal, F.Cu at (103.3, 112.0)
- added REF**: , pad:universal, F.Cu at (103.3, 109.5)
- added REF**: , pad:universal, F.Cu at (95.7, 109.5)
- added REF**: , pad:universal, F.Cu at (98.2, 112.0)
- added REF**: , pad:universal, F.Cu at (95.7, 112.0)
- added REF**: , pad:universal, F.Cu at (98.2, 109.5)
- added REF**: , pad:universal, F.Cu at (93.1, 112.0)
- added REF**: , pad:universal, F.Cu at (70.3, 68.9)
- added REF**: , pad:universal, F.Cu at (93.1, 109.5)
- added REF**: , pad:universal, F.Cu at (90.6, 112.0)
- added REF**: , pad:universal, F.Cu at (90.6, 109.5)
- added REF**: , pad:universal, F.Cu at (83.0, 109.5)
- added REF**: , pad:universal, F.Cu at (85.5, 109.5)
- added REF**: , pad:universal, F.Cu at (80.4, 112.0)
- added REF**: , pad:universal, F.Cu at (80.4, 109.5)
- added REF**: , pad:universal, F.Cu at (83.0, 114.6)
- added REF**: , pad:universal, F.Cu at (80.4, 114.6)
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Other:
- board size 50 x 50 mm -> 100 x 100 mm
